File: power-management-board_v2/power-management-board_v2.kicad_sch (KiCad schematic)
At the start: 127 parts, among them IC2 TLP7820_TP4,E, IC3 MCP2562, J1 Conn_01x02, J2 Conn_01x02, J3 Conn_01x04, J4 Conn_01x04, J5 Conn_01x04_Pin, J6 Conn_01x02_Pin, J7 Conn_01x02, J8 Conn_01x02, J9 Conn_01x02, K1 FBR562ND12-W, Q3 SSM3K341R, Q4 SSM3K341R, SW1 SW_Push, SW3 SW_SPDT_312, U1 TLP293, U2 TPS54560BDDA, U3 STM32G431K8Tx, U4 NJM12888F33, U5 TLP293, U6 CZ3A07, U7 AP7375, U8 TLP293

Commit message: 完成
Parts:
- added D10: SS2040FL, 0Ikedalibrary:SOD-123FL, symbol Device:D
- added D8: LED, LED_SMD:LED_0603_1608Metric_Pad1.05x0.95mm_HandSolder, symbol Device:LED
- added JP1: Jumper_2_Open, Connector_PinHeader_2.54mm:PinHeader_1x02_P2.54mm_Vertical, symbol Jumper:Jumper_2_Open
- added R34, R40, R41: 10k, Resistor_SMD:R_0603_1608Metric_Pad0.98x0.95mm_HandSolder, symbol Device:R
- added U9: TLP293, Package_SO:SOIC-4_4.55x2.6mm_P1.27mm, symbol Isolator:TLP293
- K1: footprint GN10_Parts:FBR562 -> 0Ikedalibrary:FBR562ND12-W
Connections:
- net +12VA: now also JP1.2 (B)
- net +3.3V: now also R40.2
- net GATE_A: now also JP1.1 (A)
- net GND: now also R34.1; no longer C2.2, C27.2
- net GNDA: now also D8.1 (K)
- net GNDD: now also U9.3
- net GNDPWR: now also C2.2, C27.2
- net INPUT_relay: now also D10.1 (K), U9.1
- net IP: now also K1.10 (COM); no longer K1.5 (COM)
- net VCC: now also R41.1
- net at R11.1, R12.1, R13.1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: now also K1.7 (N.C.); no longer K1.2 (N.C.)
- net at R26.2, R30.2, R47.2: now also K1.5 (COM); no longer K1.10 (COM)
- net at D29.2 (A), Q3.3 (D): now also K1.9 (coil_2); no longer K1.4 (coil_2)
- net at R46.1: now also K1.2 (N.C.); no longer K1.7 (N.C.)
- net at D30.2 (A), Q4.3 (D): now also K1.4 (coil_2); no longer K1.9 (coil_2)
- net VCC_check: now reaches U3.28 (PB5)
- net VCC_check: now also R40.1, U9.4
- new net: D8.2 (A), R41.2
- new net: D10.2 (A), R34.2, U9.2
- no-connect marks 9 -> 8
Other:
- moved on the sheet: D6, D7, D9, K1A, K1B, R27, R31, R32, R33, R48, R49, U1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

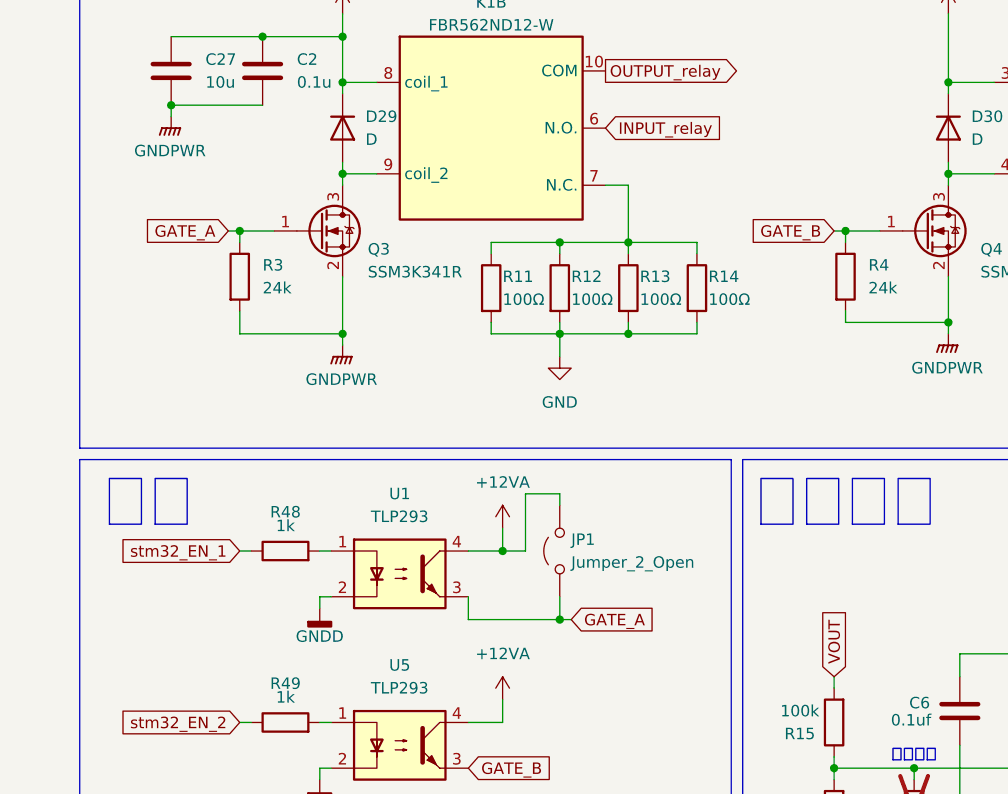
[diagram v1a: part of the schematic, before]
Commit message: feat:ゲートに抵抗追加＆常時ON削除
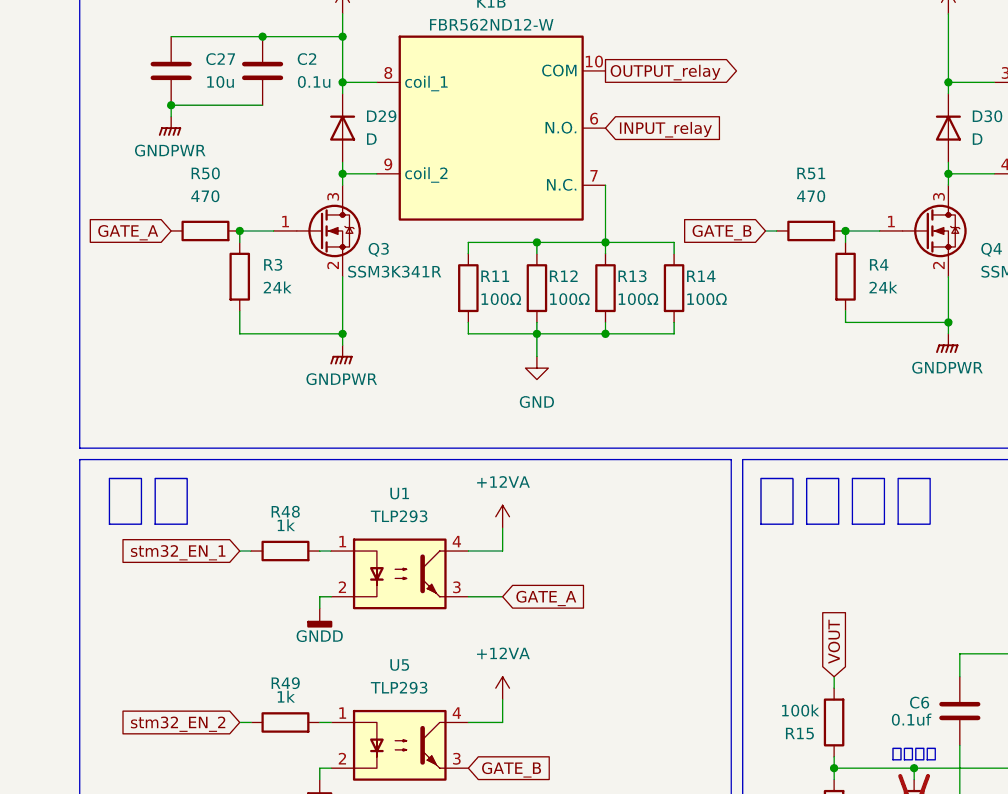
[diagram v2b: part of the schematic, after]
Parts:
- removed JP1: Jumper_2_Open, Connector_PinHeader_2.54mm:PinHeader_1x02_P2.54mm_Vertical, symbol Jumper:Jumper_2_Open
- added R50, R51: 470, Resistor_SMD:R_0603_1608Metric_Pad0.98x0.95mm_HandSolder, symbol Device:R
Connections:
- net GATE_A: now also R50.1; no longer Q3.1 (G), R3.1
- net GATE_B: now also R51.1; no longer Q4.1 (G), R4.1
- new net: Q3.1 (G), R3.1, R50.2
- new net: Q4.1 (G), R4.1, R51.2
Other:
- moved on the sheet: R11, R12, R13, R14
